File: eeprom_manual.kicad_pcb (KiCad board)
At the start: 2 copper layers, 48.5 x 94.2 mm, 45 parts, among them J1 Barrel_Jack, J2 Conn_01x02, SW1 SW_SPST, SW2 SW_DIP_x08, SW3 SW_DIP_x10, SW4 SW_DIP_x01, U1 L7805, U2 74HC245, U3 M54513FP, U4 28C16

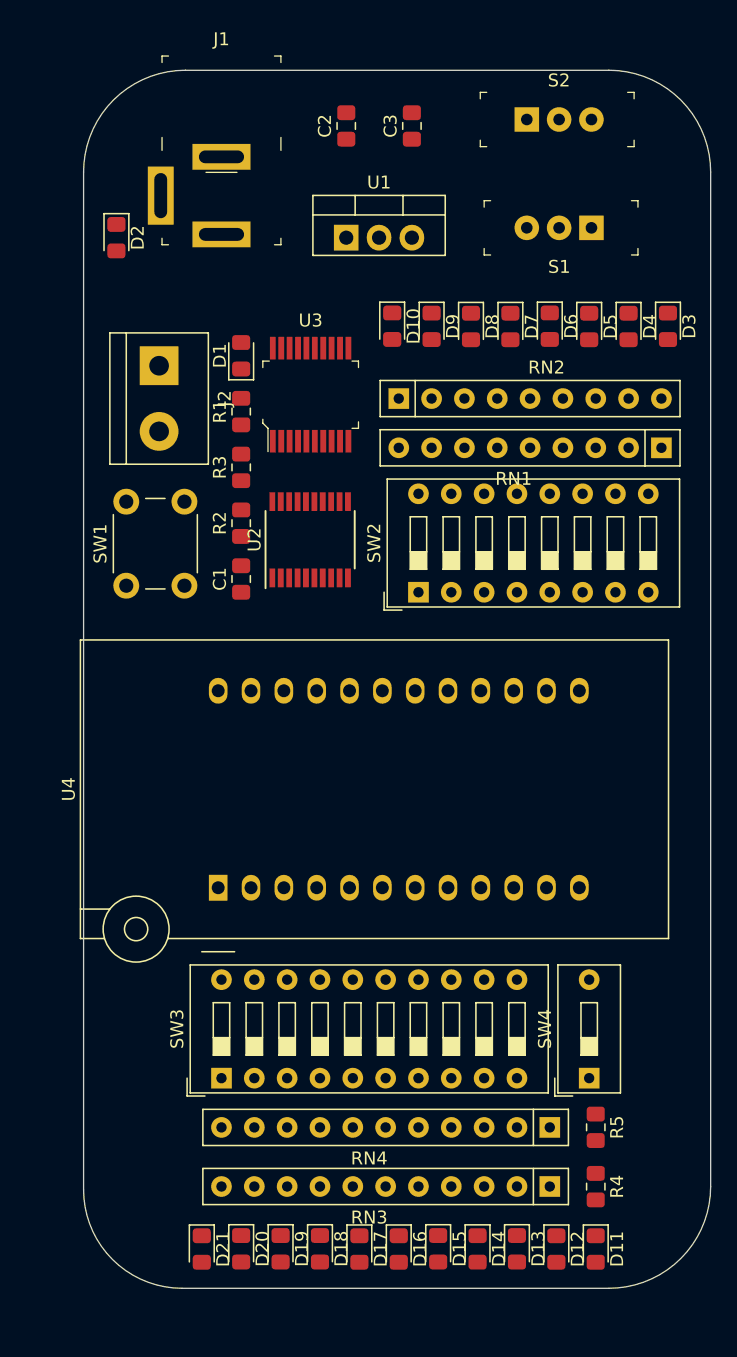
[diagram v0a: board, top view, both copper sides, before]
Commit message: Added traces to pcb
- pcbnew component layout adjustments
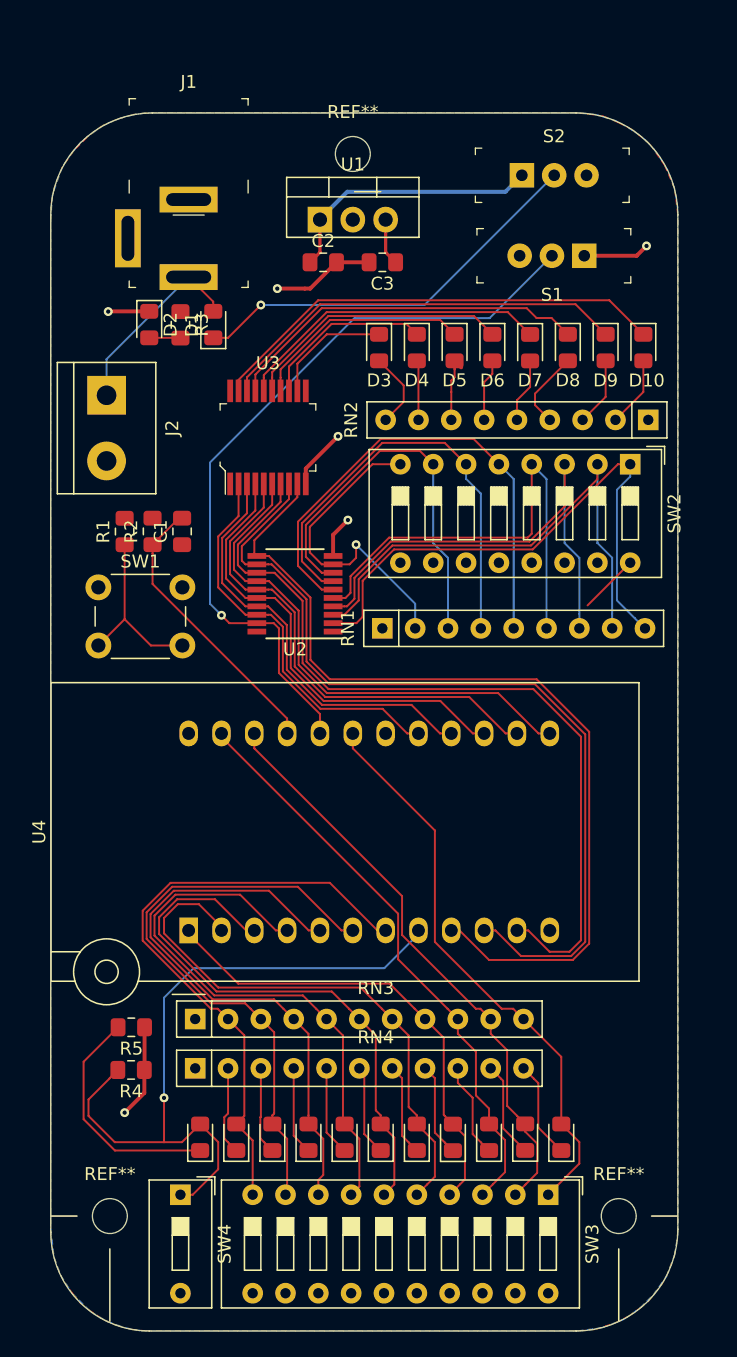
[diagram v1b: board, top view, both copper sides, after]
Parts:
- added REF**: MountingHole_2.7mm_M2.5_ISO14580, MountingHole:MountingHole_2.7mm_M2.5_ISO14580, F.Cu at (32.3, 105.7)
- added REF**: MountingHole_2.7mm_M2.5_ISO14580, MountingHole:MountingHole_2.7mm_M2.5_ISO14580, F.Cu at (71.6, 105.7)
- added REF**: MountingHole_2.7mm_M2.5_ISO14580, MountingHole:MountingHole_2.7mm_M2.5_ISO14580, F.Cu at (51.1, 23.5)
- D2: value LED -> PWR
- S1: value EG1218 -> IN/OUT
- S2: value EG1218 -> ON/OFF
- moved R4 37.1 mm to (33.9, 94.4), turned to 180 degrees
- moved R5 36.8 mm to (33.9, 91.1), turned to 180 degrees
- moved SW4 32.9 mm to (37.7, 104.0), turned to 270 degrees
- moved D11 31.8 mm to (39.2, 99.6), turned to 90 degrees
- moved RN3 30.3 mm to (38.9, 90.4), turned to 0 degrees
- moved D21 29.1 mm to (67.2, 99.6), turned to 90 degrees
- moved RN4 27.8 mm to (38.9, 94.2), turned to 0 degrees
- moved SW3 26.8 mm to (66.2, 104.0), turned to 270 degrees
- moved D12 26.2 mm to (42.0, 99.6), turned to 90 degrees
- moved RN1 25.7 mm to (53.3, 60.2), turned to 0 degrees
- moved D20 23.6 mm to (64.4, 99.6), turned to 90 degrees
- moved D3 22.4 mm to (53.1, 38.5)
- moved D13 20.8 mm to (44.8, 99.6), turned to 90 degrees
- moved D10 19.5 mm to (73.5, 38.5)
- moved RN2 19.4 mm to (73.9, 44.1), turned to 180 degrees
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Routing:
- net Net-(U2-Pad11): track 0.00 -> 69.7 mm
- net Net-(U2-Pad12): track 0.00 -> 67.6 mm
- net Net-(U2-Pad13): track 0.00 -> 64.3 mm
- net OE: track 0.00 -> 59.6 mm, vias 0 -> 1
- net Net-(D11-Pad2): track 0.00 -> 55.6 mm, vias 0 -> 1
- net Net-(D12-Pad2): track 0.00 -> 47.5 mm
- net Net-(D13-Pad2): track 0.00 -> 46.2 mm
- net Net-(D20-Pad2): track 0.00 -> 45.7 mm
- net Net-(D19-Pad2): track 0.00 -> 45.5 mm
- net Net-(D14-Pad2): track 0.00 -> 45.3 mm
- net Net-(D15-Pad2): track 0.00 -> 44.5 mm
- net Net-(D21-Pad2): track 0.00 -> 44.5 mm
- net Net-(RN1-Pad9): track 0.00 -> 43.7 mm
- net Net-(D16-Pad2): track 0.00 -> 43.5 mm
- net Net-(D17-Pad2): track 0.00 -> 43.0 mm
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- added copper zone on F.Cu, net +5V
- added copper zone on B.Cu, net GND
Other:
- net class Default: clearance 0.2 -> 0.2032; trace_width 0.25 -> 0.3048; via_dia 0.8 -> 0.6858; via_drill 0.4 -> 0.3302
- rule pad_to_mask_clearance: 0.051 -> 0.0508
- rule trace_clearance: 0.2 -> 0.2032
- rule trace_min: 0.2 -> 0.1524
- rule via_min_drill: 0.3 -> 0.254
- rule via_min_size: 0.4 -> 0.508

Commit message: Add silkscreen labels, Clean up traces
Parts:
- D2: value PWR -> D2
- S1: value IN/OUT -> READ/WRITE
- moved D2 4.71 mm to (30.7, 35.6)
- moved C2 1.78 mm to (48.8, 33.7)
- moved C3 1.78 mm to (53.3, 33.7)
- moved U1 1.78 mm to (48.5, 30.4)
- moved REF** 0.51 mm to (31.8, 105.7)
- moved REF** 0.51 mm to (72.1, 105.7)
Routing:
- net GND: track 31.5 -> 20.3 mm, vias 6 -> 3
- net +5V: track 8.29 -> 0.00 mm
- net Net-(D19-Pad2): track 45.5 -> 52.9 mm
- net Net-(D20-Pad2): track 45.7 -> 52.8 mm
- net Net-(D18-Pad2): track 36.7 -> 43.2 mm
- net Net-(D14-Pad2): track 45.3 -> 51.1 mm
- net Net-(D13-Pad2): track 46.2 -> 52.0 mm
- net Net-(D16-Pad2): track 43.5 -> 49.2 mm
- net Net-(D15-Pad2): track 44.5 -> 50.2 mm
- net Net-(D12-Pad2): track 47.5 -> 52.9 mm
- net Net-(D17-Pad2): track 43.0 -> 48.4 mm
- net Net-(D2-Pad2): track 2.42 -> 7.46 mm
- net Net-(D21-Pad2): track 44.5 -> 49.0 mm
- net Net-(R1-Pad1): track 13.9 -> 16.1 mm
- net Net-(RN1-Pad9): track 43.7 -> 42.2 mm
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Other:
- board text added: "ADDRESS"
- board text added: "BYTE_WRITE"
- board text added: "DATA"
- board text added: "EEPROM"
- board text added: "ON/OFF"
- board text added: "PWR"
- board text added: "R/W"
